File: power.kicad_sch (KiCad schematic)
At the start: 37 parts, among them U2 LMR51635XDDCR, U3 AMS1117

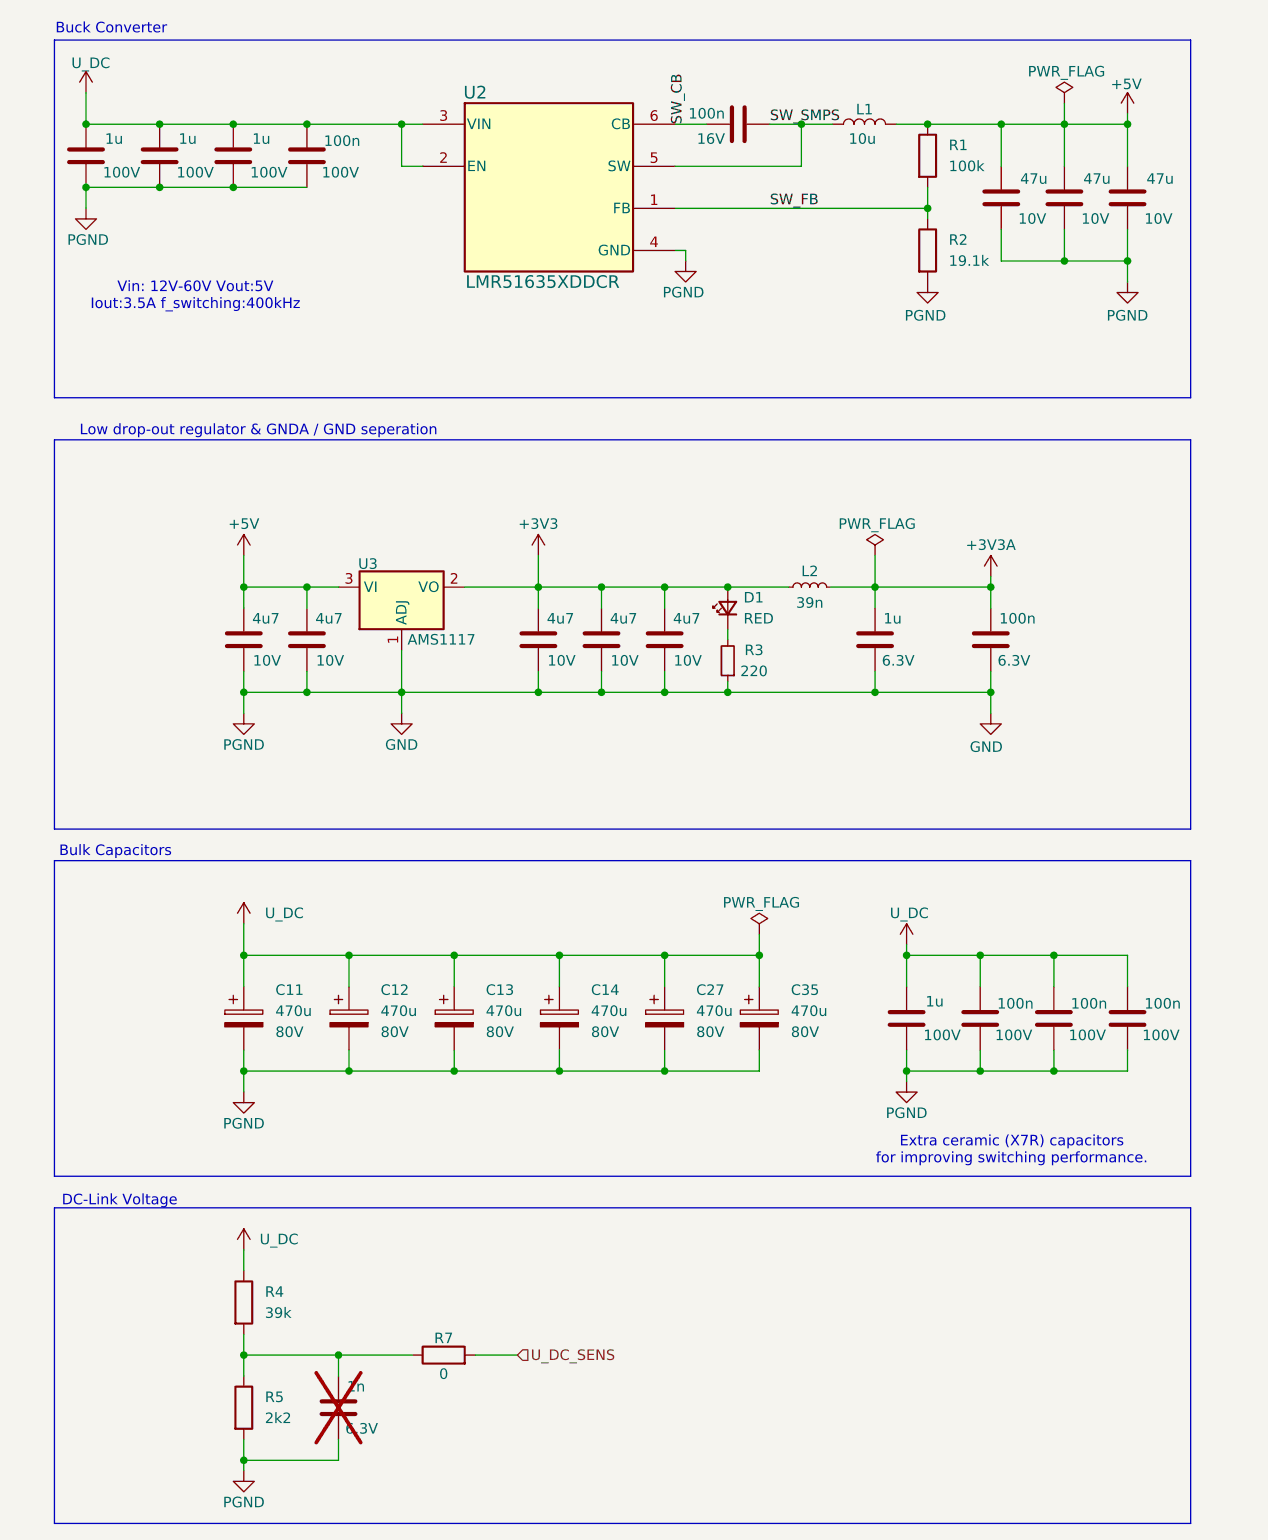
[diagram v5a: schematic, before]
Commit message: ERC errors have been fixed. XTAL changed to 12MHz. WiP DRC errors.
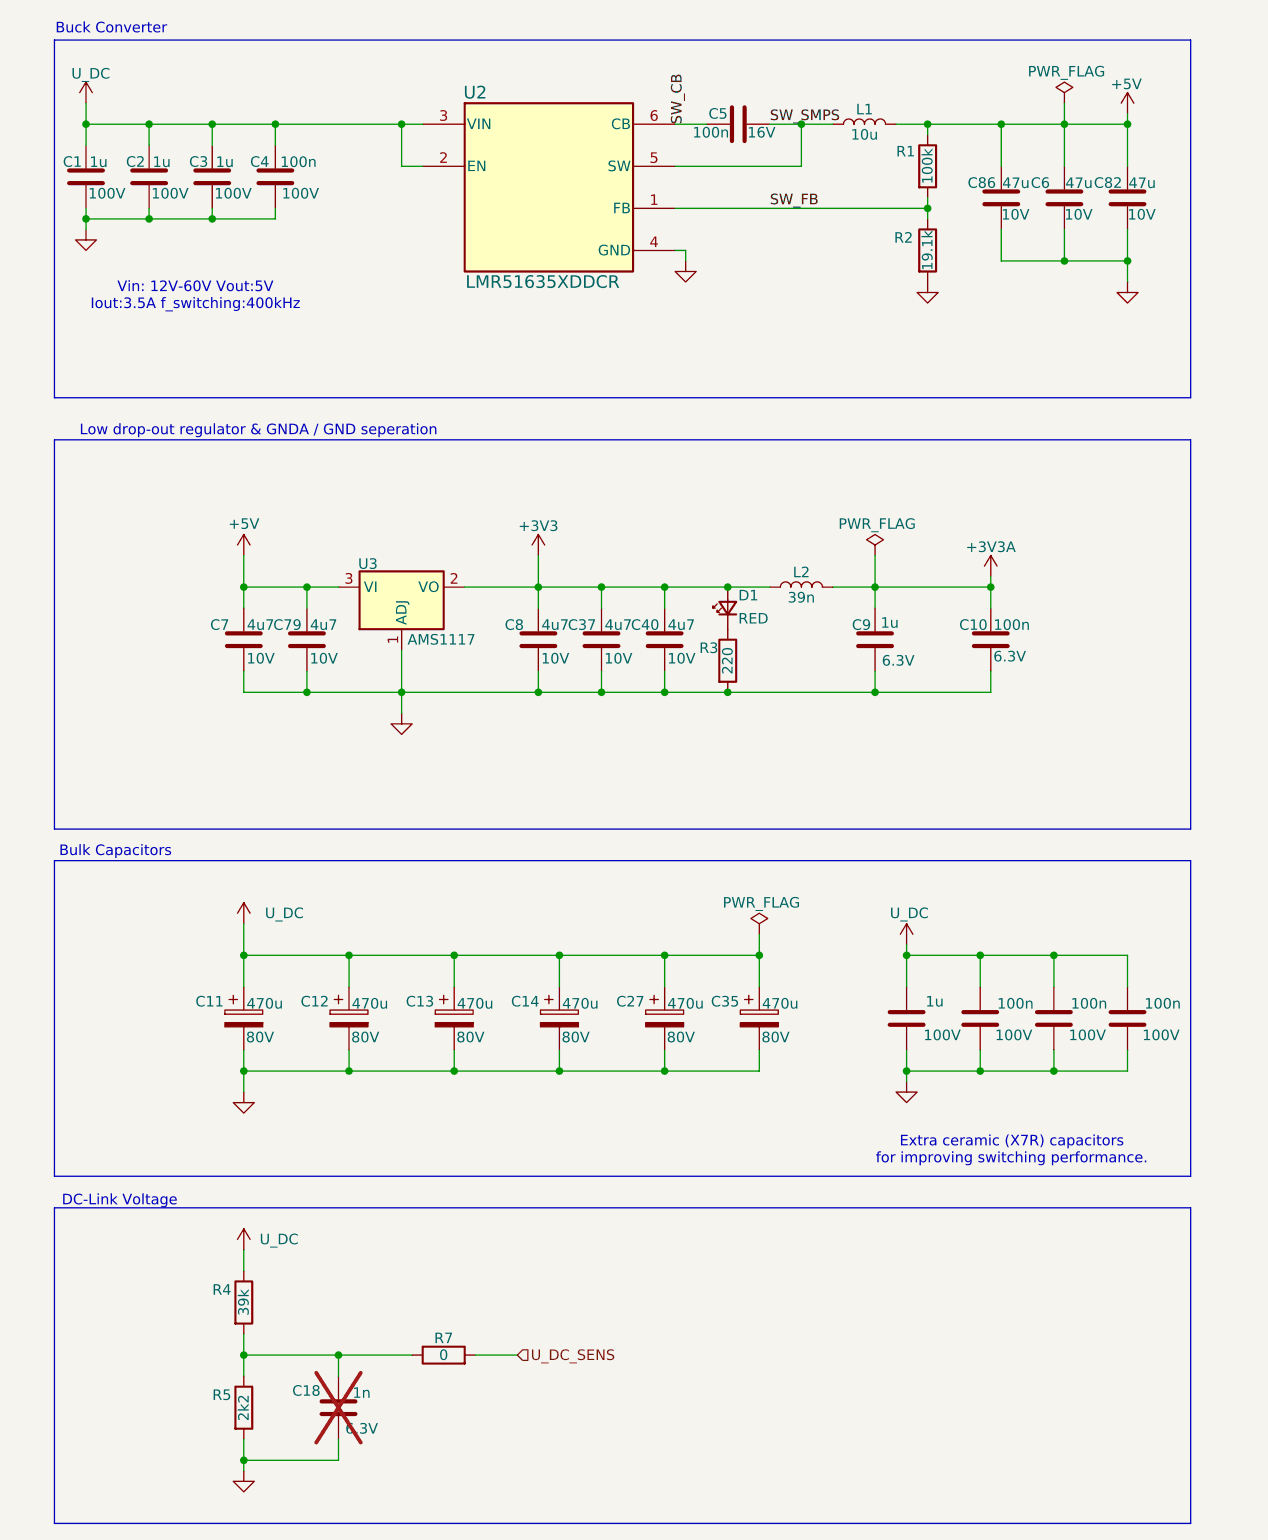
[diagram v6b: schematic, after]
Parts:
- removed L2: 39n, Inductor_SMD:L_0603_1608Metric, symbol Device:L_Small
- removed R1: 100k, Resistor_SMD:R_0402_1005Metric, symbol NanoGaN:R
- removed R2: 19.1k, Resistor_SMD:R_0402_1005Metric, symbol NanoGaN:R
- removed R3: 220, Resistor_SMD:R_0402_1005Metric, symbol Device:R_Small
- removed R4: 39k, Resistor_SMD:R_0603_1608Metric, symbol NanoGaN:R
- removed R5: 2k2, Resistor_SMD:R_0402_1005Metric, symbol NanoGaN:R
- removed R7: 0402WGF0000TCE, Resistor_SMD:R_0402_1005Metric, symbol NanoGaN:R
- added L2: FHW0603UC039JST, Inductor_SMD:L_0603_1608Metric, symbol Device:L
- added R1: 0402WGF1003TCE, Resistor_SMD:R_0402_1005Metric, symbol Device:R
- added R2: 0402WGF1912TCE, Resistor_SMD:R_0402_1005Metric, symbol Device:R
- added R3: 0402WGF2200TCE, Resistor_SMD:R_0402_1005Metric, symbol Device:R
- added R4: 0603WAF3902T5E, Resistor_SMD:R_0603_1608Metric, symbol Device:R
- added R5: 0402WGF2201TCE, Resistor_SMD:R_0402_1005Metric, symbol Device:R
- added R7: 0402WGF0000TCE, Resistor_SMD:R_0402_1005Metric, symbol Device:R
- C1, C2, C3: value 1u -> CL31B105KCHNNNE; Capacitance (none) -> 1u
- C10: value 100n -> 0402B104K6R3CT; Capacitance (none) -> 100n
- C11, C12, C13, C14, C27, C35: value 470u -> EKYC800ELL471MK25S; Capacitance (none) -> 470u
- C18: value 1n -> ~; Capacitance (none) -> 1n
- C37, C40, C7, C79, C8: value 4u7 -> CL05A475MP5NRNC; Capacitance (none) -> 4u7
- C4: value 100n -> CL21B104KCFNNNE; Capacitance (none) -> 100n; Manufacturer_Name SAMSUNG -> (none); Manufacturer_Part_Number CL21B104KCFNNNE -> (none)
- C5: value 100n -> CL05B104KO5NNNC; Capacitance (none) -> 100n; Manufacturer_Part_Number CL05B104KO5NNNC -> (none)
- C6, C82, C86: value 47u -> CL31A476MPHNNNE; Capacitance (none) -> 47u
- C9: value 1u -> CL05B105KQ5NQNC; Capacitance (none) -> 1u
- L1: value 10u -> XAL6060-103ME; Inductance (none) -> 10u
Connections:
- net +3V3: now also L2.1
- net +3V3A: now also L2.2
- net +5V: now also R1.1
- net GND: now also R2.2, R3.2, R5.2
- net SW_FB: now also R1.2, R2.1
- net U_DC: now also R4.1
- net U_DC_SENS: now also R7.2
- net at D1.1 (K): now also R3.1
- net at C18.1: now also R4.2, R5.1, R7.1

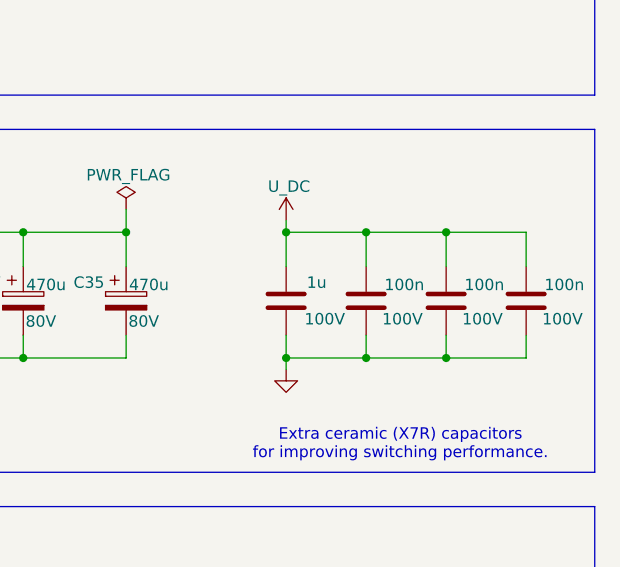
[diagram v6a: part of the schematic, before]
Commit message: fixed all ERC and DRC errors/warnings, now in review stage.
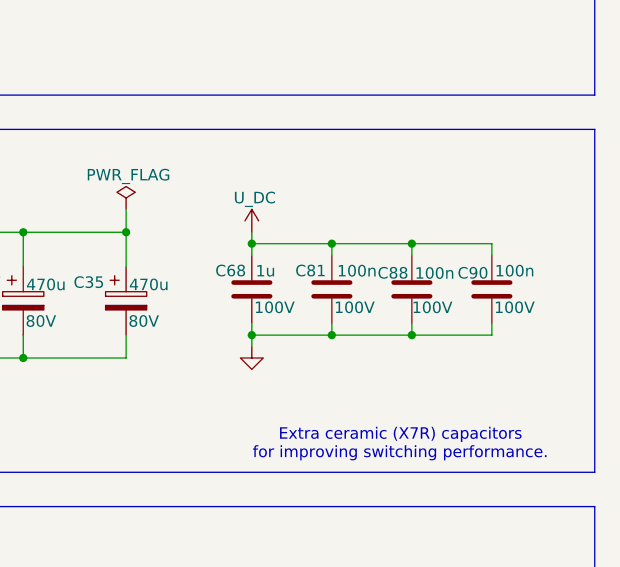
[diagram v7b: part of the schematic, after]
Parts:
- C11, C12, C13, C14, C27, C35: footprint Capacitor_THT:CP_Radial_D12.5mm_P5.00mm -> NanoGaN:CP_Radial_D12.5mm_P5.00mm
- C68: value 1u -> CL31B105KCHNNNE; Capacitance (none) -> 1u
- C81, C88, C90: value 100n -> CL21B104KCFNNNE; Capacitance (none) -> 100n

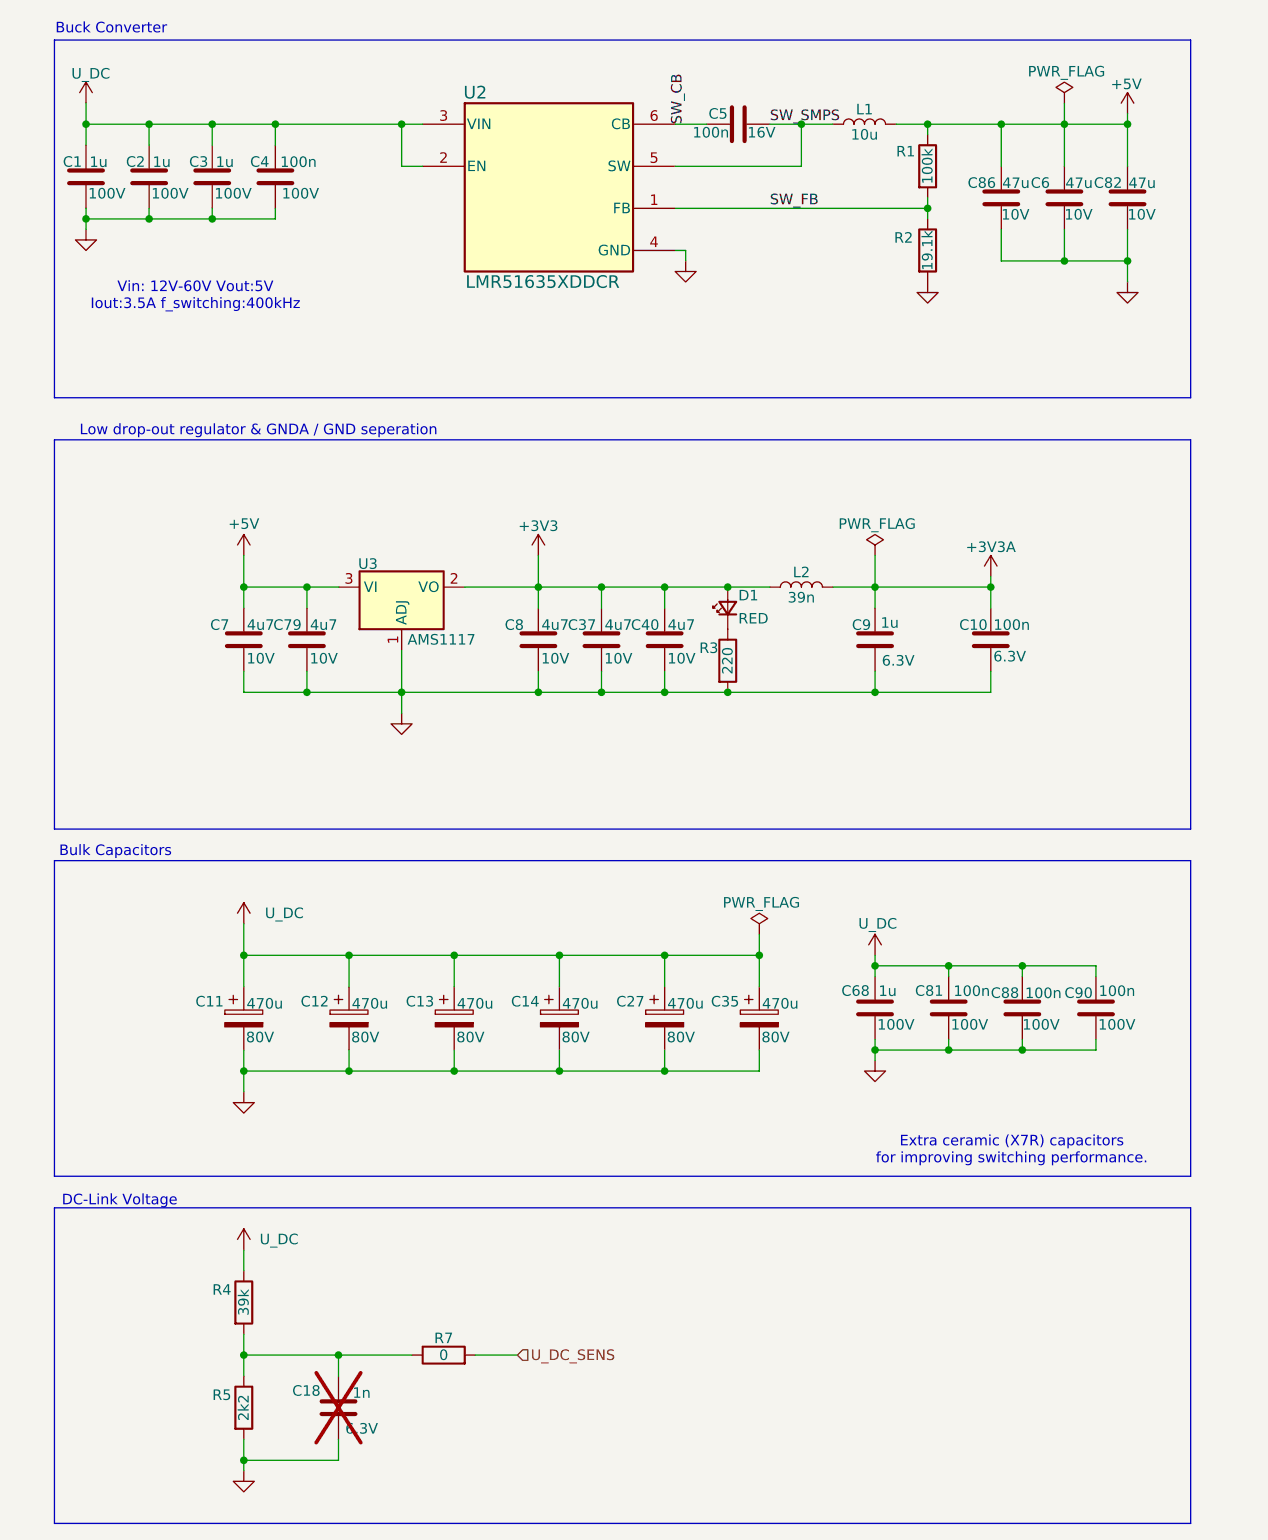
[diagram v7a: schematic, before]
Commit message: added leds and buttons
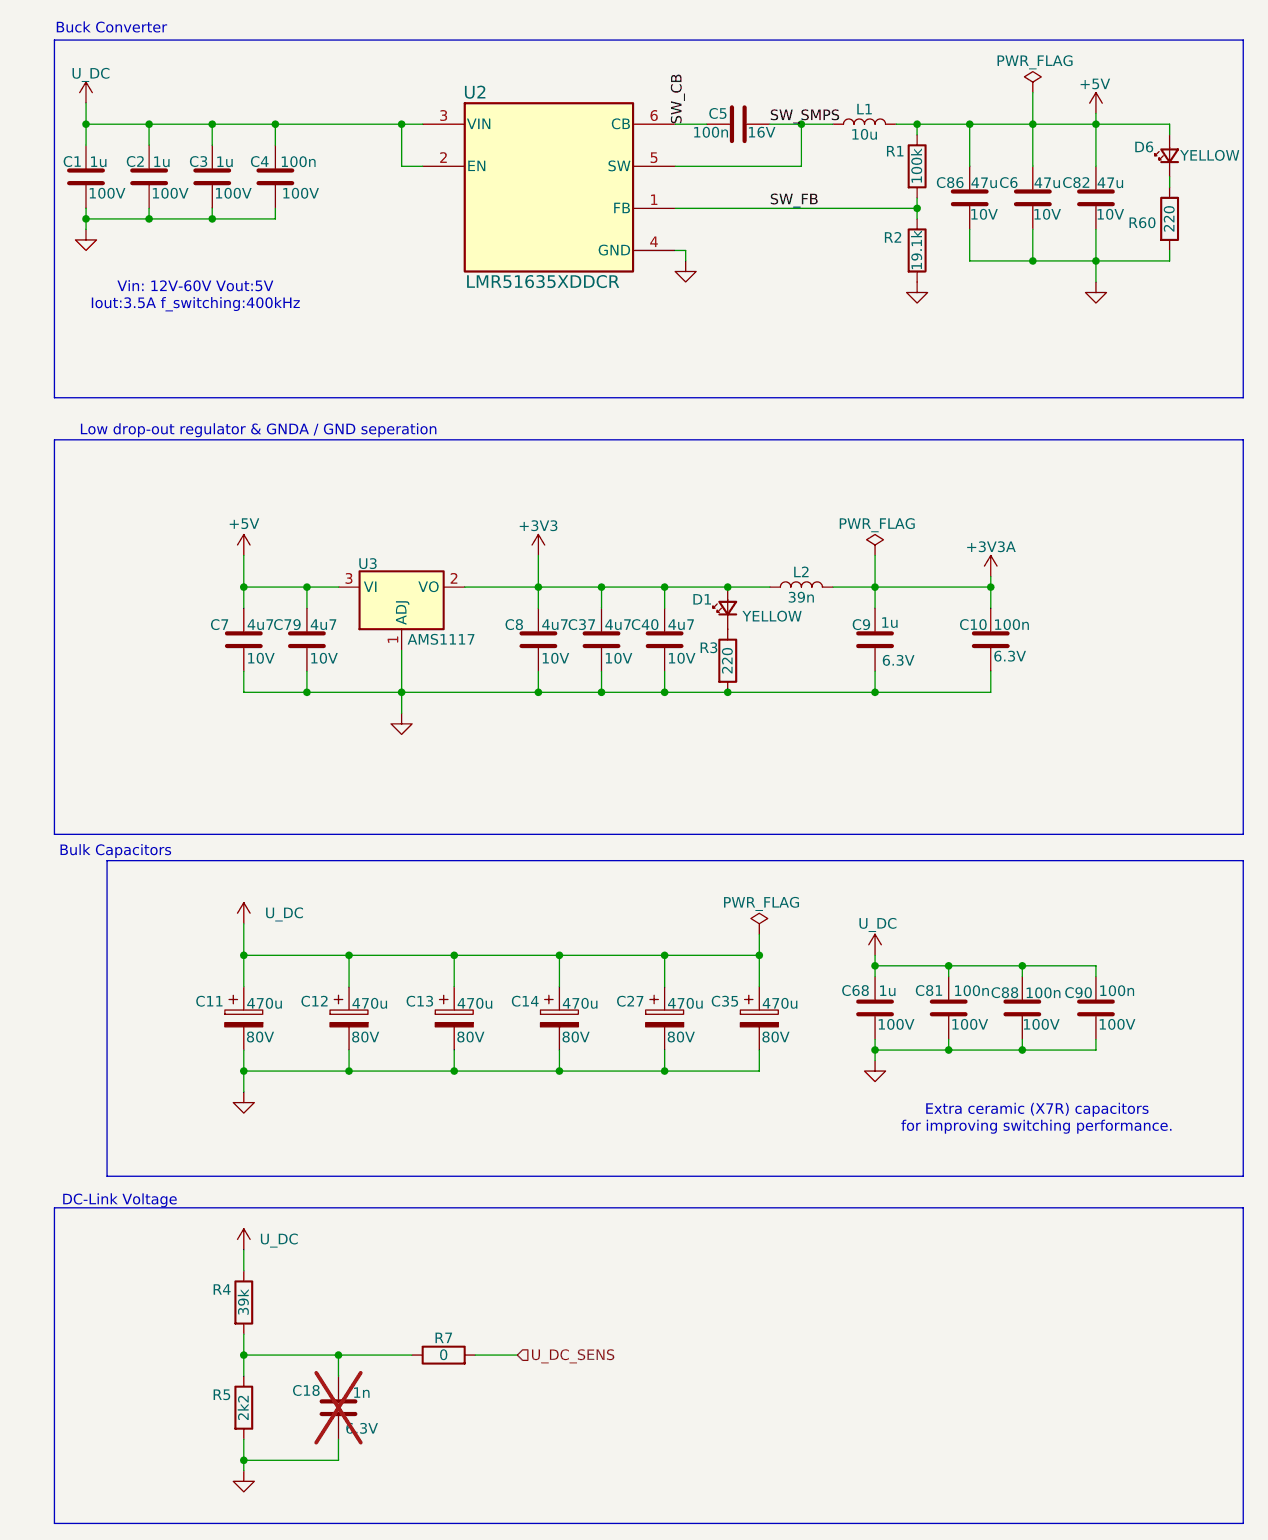
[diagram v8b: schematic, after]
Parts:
- added D6: YELLOW, LED_SMD:LED_0805_2012Metric, symbol Device:LED_Small
- added R60: 0402WGF2200TCE, Resistor_SMD:R_0402_1005Metric, symbol Device:R
- D1: value RED -> YELLOW; LCSC C84256 -> C2296
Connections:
- net +5V: now also D6.2 (A)
- net GND: now also R60.2
- new net: D6.1 (K), R60.1
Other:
- moved on the sheet: C6, C82, C86, R1, R2
